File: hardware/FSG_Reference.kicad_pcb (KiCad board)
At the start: 4 copper layers, 63.5 x 38 mm, 72 parts, among them J2 D369-G99-NP4, K1 SANYOU_SRD_Form_C, Q1 BSS138, Q2 Si2319CDS, Q3 BSS138, U1 LM393, U2 LM393, U3 LM393, U4 MC78M12CDTG DPAK, U5 LM393, U6 74AHC1G02, U7 LM1117-5.0

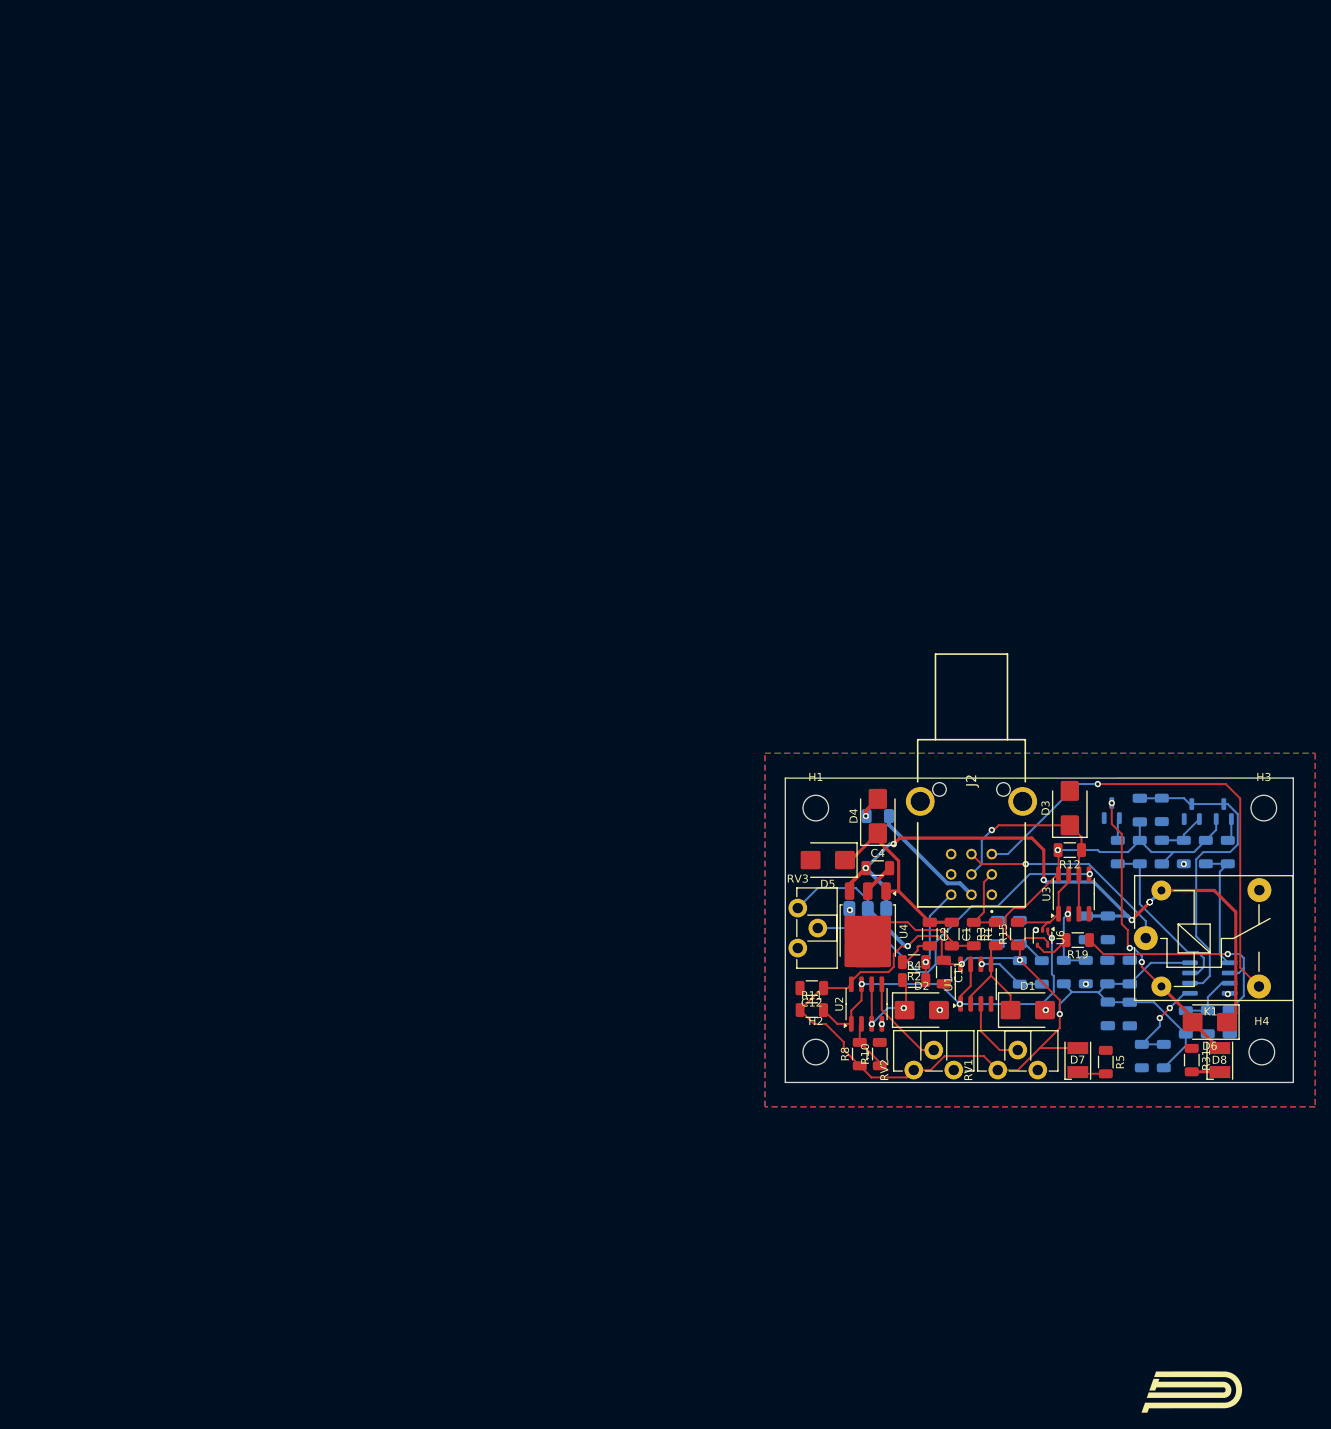
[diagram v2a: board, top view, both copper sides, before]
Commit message: New BSPD Layout based on BSPD by Jakub Drankiewicz in 2021
-Schematic needs to be adjusted for better understanding
-Comparator of Current Sensor removed, the one on Current Sensor Board is sufficient
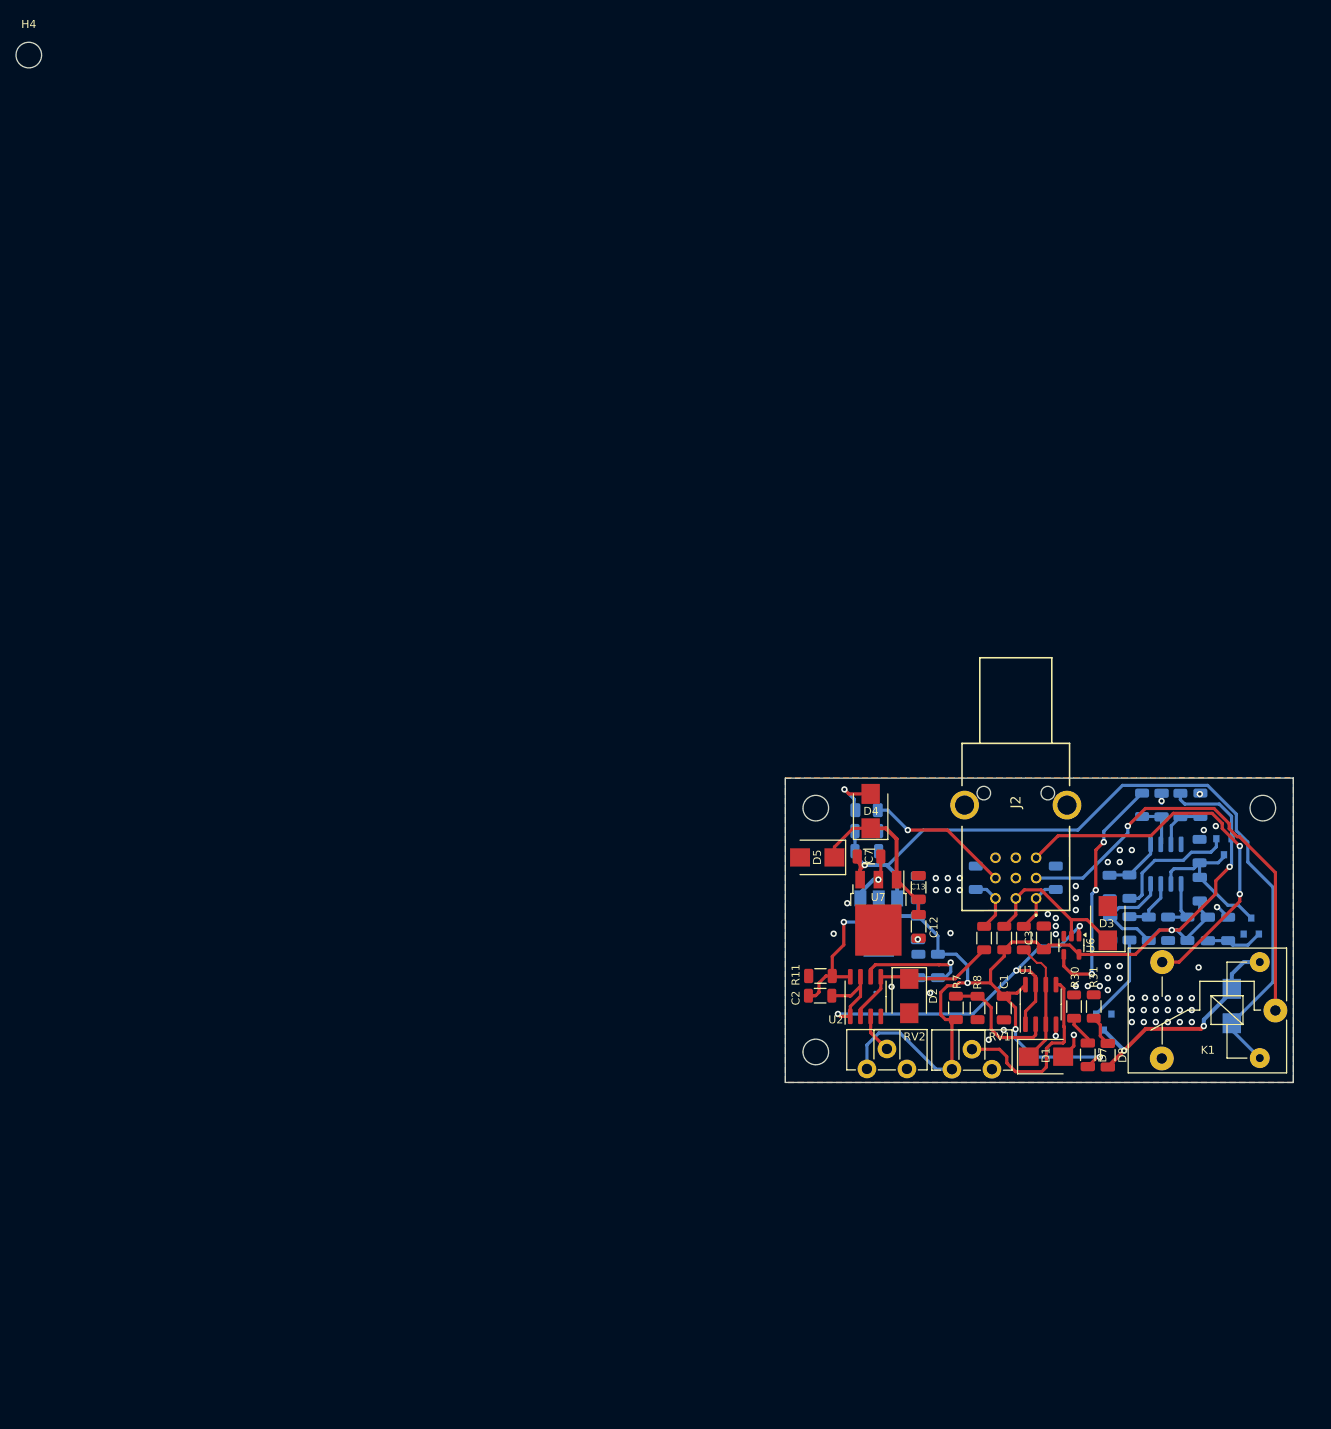
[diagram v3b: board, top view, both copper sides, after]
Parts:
- removed C14: 100n, Capacitor_SMD:C_1206_3216Metric
- removed R14, R15: 10k, Resistor_SMD:R_1206_3216Metric
- removed R16, R9: 0R, Resistor_SMD:R_1206_3216Metric
- removed R2: 100k, Resistor_SMD:R_1206_3216Metric
- removed R5: 1k, Resistor_SMD:R_1206_3216Metric
- removed RV3: 20k, Potentiometer_THT:Potentiometer_ACP_CA9-H2,5_Horizontal
- removed U3: LM393, Package_SO:SOIC-8_3.9x4.9mm_P1.27mm
- added C15: 100n, Capacitor_SMD:C_1206_3216Metric, B.Cu at (107.9, 102.6)
- added R30: 1k, Resistor_SMD:R_1206_3216Metric, F.Cu at (133.8, 122.1)
- C1: value 10u -> 100n
- C11, D6, G***, R1, R12, R19: moved to B.Cu
- C12: value 100n -> 10u
- C13: value 10u -> 100n; moved to F.Cu
- C3, C7: moved to F.Cu
- C4: value 100n -> 10u; moved to B.Cu
- D7, D8: footprint LED_SMD:LED_PLCC-2 -> Capacitor_SMD:C_1206_3216Metric
- R10, R4: value 10k -> 100k; moved to B.Cu
- R13, R6: value 100k -> 10k; moved to F.Cu
- R7: value 10k -> 100k; moved to F.Cu
- R8: value 100k -> 10k
- U4: value MC78M12CDTG DPAK -> LM1117-5.0; footprint Package_TO_SOT_SMD:TO-252-3_TabPin2 -> Package_TO_SOT_SMD:SOT-223; moved to B.Cu
- U6: footprint Package_TO_SOT_SMD:SOT-353_SC-70-5 -> Package_TO_SOT_SMD:SOT-23-5
- U7: value LM1117-5.0 -> MC78M12CDTG DPAK; footprint Package_TO_SOT_SMD:SOT-223 -> Package_TO_SOT_SMD:TO-252-3_TabPin2; moved to F.Cu
- moved H4 198.2 mm to (3.12, 3.12)
- moved G*** 61.1 mm to (126.5, 113.0), turned to 180 degrees
- moved C7 33.1 mm to (108.2, 103.3), turned to 0 degrees
- moved C13 28.4 mm to (114.4, 107.2), turned to 90 degrees
- moved C5 28.4 mm to (144.7, 96.9), turned to 90 degrees
- moved R21 27.2 mm to (147.1, 96.9), turned to -90 degrees
- moved R22 27.2 mm to (149.6, 96.8), turned to 90 degrees
- moved Q3 26.5 mm to (137.5, 124.0), turned to -90 degrees
- moved C9 24.2 mm to (114.3, 107.2), turned to 90 degrees
- moved R12 23.8 mm to (114.3, 117.0), turned to 90 degrees
- moved C11 21.5 mm to (138.3, 112.3)
- moved C8 21.0 mm to (114.3, 112.2)
- moved R19 18.7 mm to (142.3, 96.8), turned to 90 degrees
- moved K1 18.6 mm to (158.9, 122.5), turned to 180 degrees
- moved R24 16.2 mm to (145.5, 112.3)
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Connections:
- net BrakeLogic renamed /Comparators/Brake1Logic
- net Error renamed /Comparators/Error
- net Relay Drive Signal renamed Net-(Q3-G)
- net Relay1 renamed Relay_1
- C1 pad 1: Net-(D4-K) -> +5V
- C12 pad 1: +5V -> Net-(D4-K)
- C13 pad 1: +5V -> Net-(D4-K)
- C2 pad 1: Net-(D4-K) -> +5V
- C7 pad 1: +5V -> +12V
- C8 pad 1: +12V -> +5V
- C9 pad 1: +12V -> +5V
- D3 pad 1: ControlSignal -> Current_Sensor
- F1 pad 2: +24V -> LV_in
- J2 pad 1: unconnected-(J2-Pad1) -> Brake_1
- J2 pad 2: +24V -> Current_Sensor
- J2 pad 3: Brake1 -> Brake_2
- J2 pad 4: Brake2 -> Relay_2
- J2 pad 5: ControlSignal -> unconnected-(J2-Pad5)
- J2 pad 6: unconnected-(J2-Pad6) -> LV_in
- J2 pad 8: Relay2 -> unconnected-(J2-Pad8)
- K1 pad 1: Relay2 -> Relay_2
- R1 pad 1: Brake2 -> Brake_1
- R10 pad 1: Net-(U2A--) -> +5V
- R10 pad 2: GND -> Net-(R10-Pad2)
- R12 pad 1: ControlSignal -> Net-(R10-Pad2)
- R12 pad 2: +5V -> GND
- R13 pad 1: +5V -> Current_Sensor
- R13 pad 2: Net-(U3A--) -> +5V
- R3 pad 2: Brake2 -> Brake_1
- R4 pad 1: Net-(D2-A1) -> Brake_2
- R4 pad 2: Brake1 -> GND
- R6 pad 1: +5V -> Net-(D2-A1)
- R6 pad 2: Net-(U1B--) -> Brake_2
- R7 pad 1: Net-(U1B--) -> +5V
- R7 pad 2: GND -> Net-(U1A--)
- R8 pad 1: +5V -> Net-(U1A--)
- R8 pad 2: Net-(U2A--) -> GND
- RV1 pad 2: Net-(U1A-+) -> Net-(U1B-+)
- RV2 pad 2: Net-(U2B-+) -> unconnected-(RV2-Pad2)
- U1 pad 2: Net-(D1-A1) -> Net-(U1A--)
- U1 pad 3: Net-(U1A-+) -> Net-(D1-A1)
- U1 pad 5: Net-(D1-A1) -> Net-(U1B-+)
- U1 pad 6: Net-(U1B--) -> Net-(D1-A1)
- U2 pad 2: Net-(U2A--) -> Net-(D2-A1)
- U2 pad 3: Net-(D2-A1) -> unconnected-(RV2-Pad2)
- U2 pad 5: Net-(U2B-+) -> Net-(D2-A1)
- U2 pad 6: Net-(D2-A1) -> Net-(R10-Pad2)
- U4 pad 1: Net-(D4-K) -> GND
- U4 pad 2: GND -> +5V
- U6 pad 2: CSLogic -> Current_Sensor
- U7 pad 1: GND -> Net-(D4-K)
- U7 pad 2: +5V -> GND
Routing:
- net Relay_2: track 0.00 -> 55.1 mm, vias 0 -> 1
- net Net-(U3B-+): track 43.0 -> 0.00 mm, vias 1 -> 0
- net ControlSignal: track 28.4 -> 0.00 mm, vias 1 -> 0
- net Relay2: track 27.4 -> 0.00 mm, vias 1 -> 0
- net /Comparators/Error: track 4.56 -> 30.6 mm, vias 0 -> 3
- net Net-(U1B-+): track 0.00 -> 23.9 mm
- net Net-(U5A--): track 29.5 -> 5.93 mm, vias 1 -> 0
- net Net-(Q1-D): track 41.0 -> 19.6 mm
- net Current_Sensor: track 0.00 -> 20.7 mm
- net LV_in: track 0.00 -> 18.2 mm, vias 0 -> 1
- net +12V: track 87.5 -> 105.3 mm, vias 7 -> 1
- net Net-(R10-Pad2): track 0.00 -> 17.7 mm, vias 0 -> 1
- net +5V: track 200.9 -> 184.4 mm, vias 5 -> 6
- net Net-(U1A--): track 0.00 -> 15.2 mm
- net +24V: track 15.0 -> 0.00 mm
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- removed copper zone on In1.Cu, net GND
- removed copper zone on In2.Cu, net GND
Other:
- copper layers 4 -> 2
